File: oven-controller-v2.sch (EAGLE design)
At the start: 28 parts, among them Q1 IRFL310, Q2 IRFL310, U1 ARDUINO_SHIELDLONGPADS

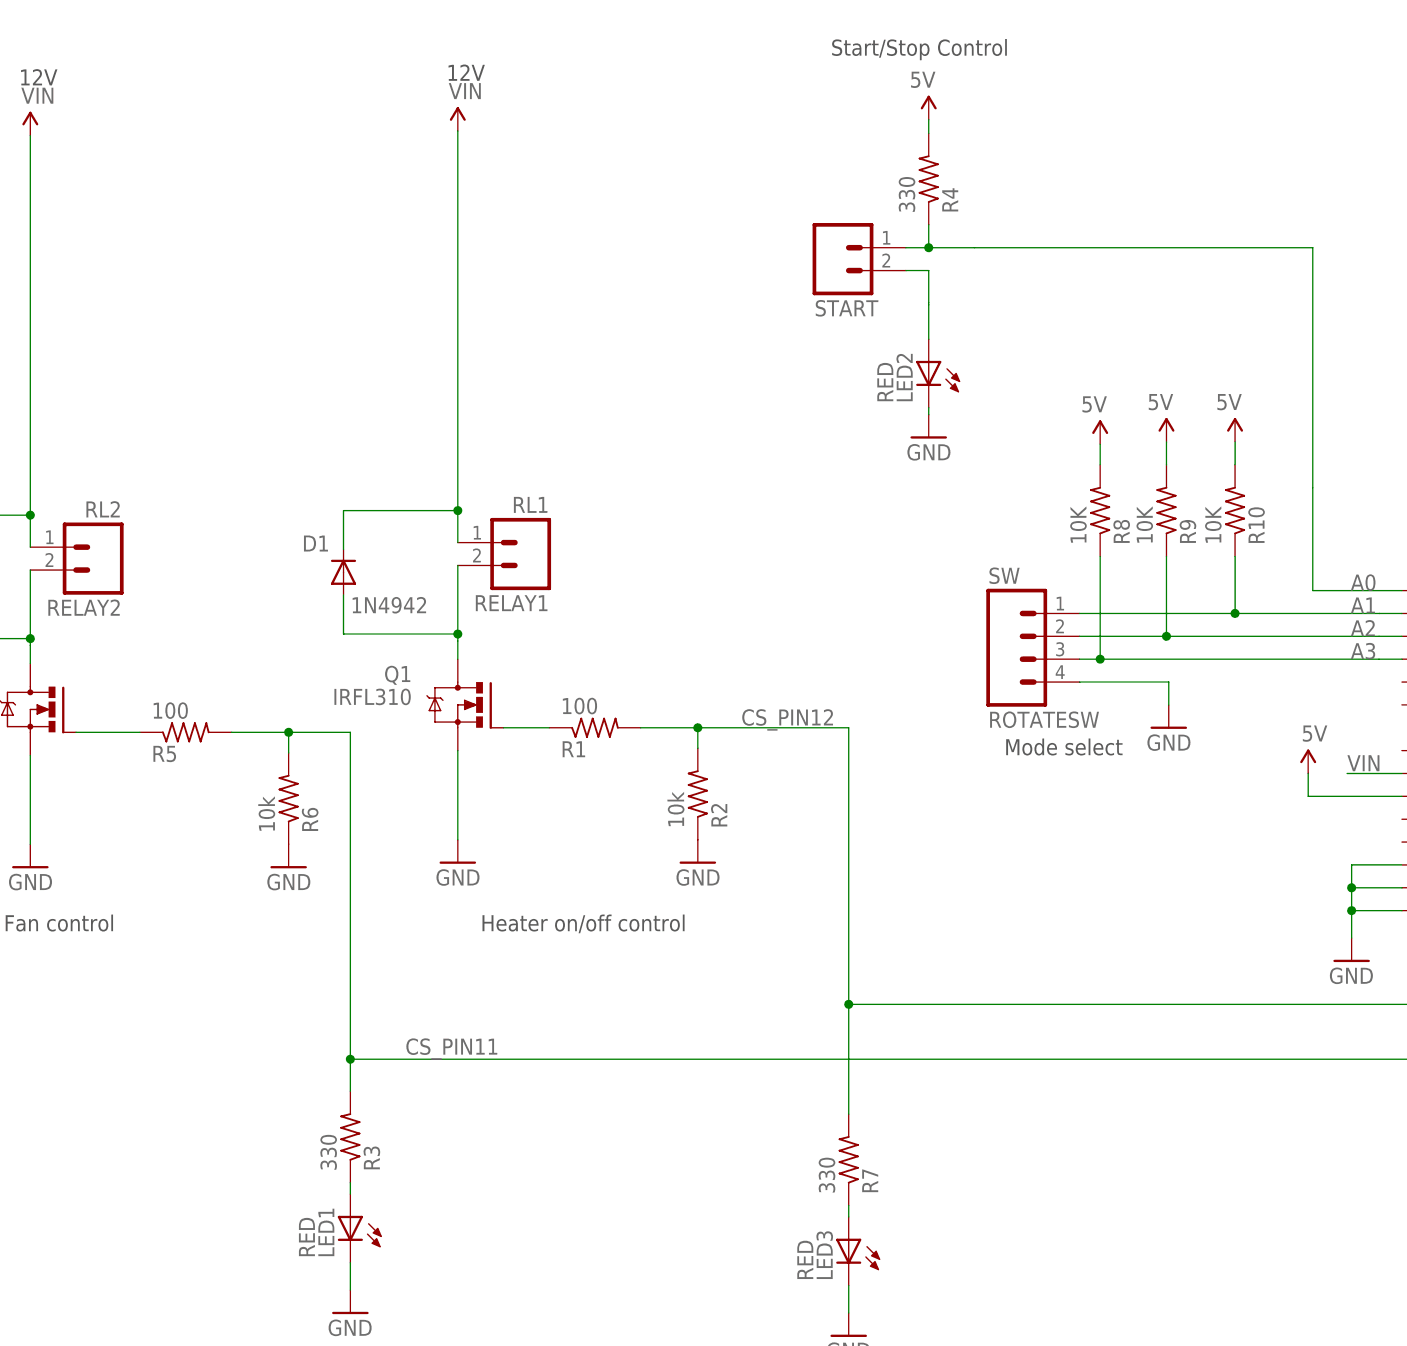
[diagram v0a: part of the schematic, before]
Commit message: Started board layout. Made resistors Sparkfun axial footprint.
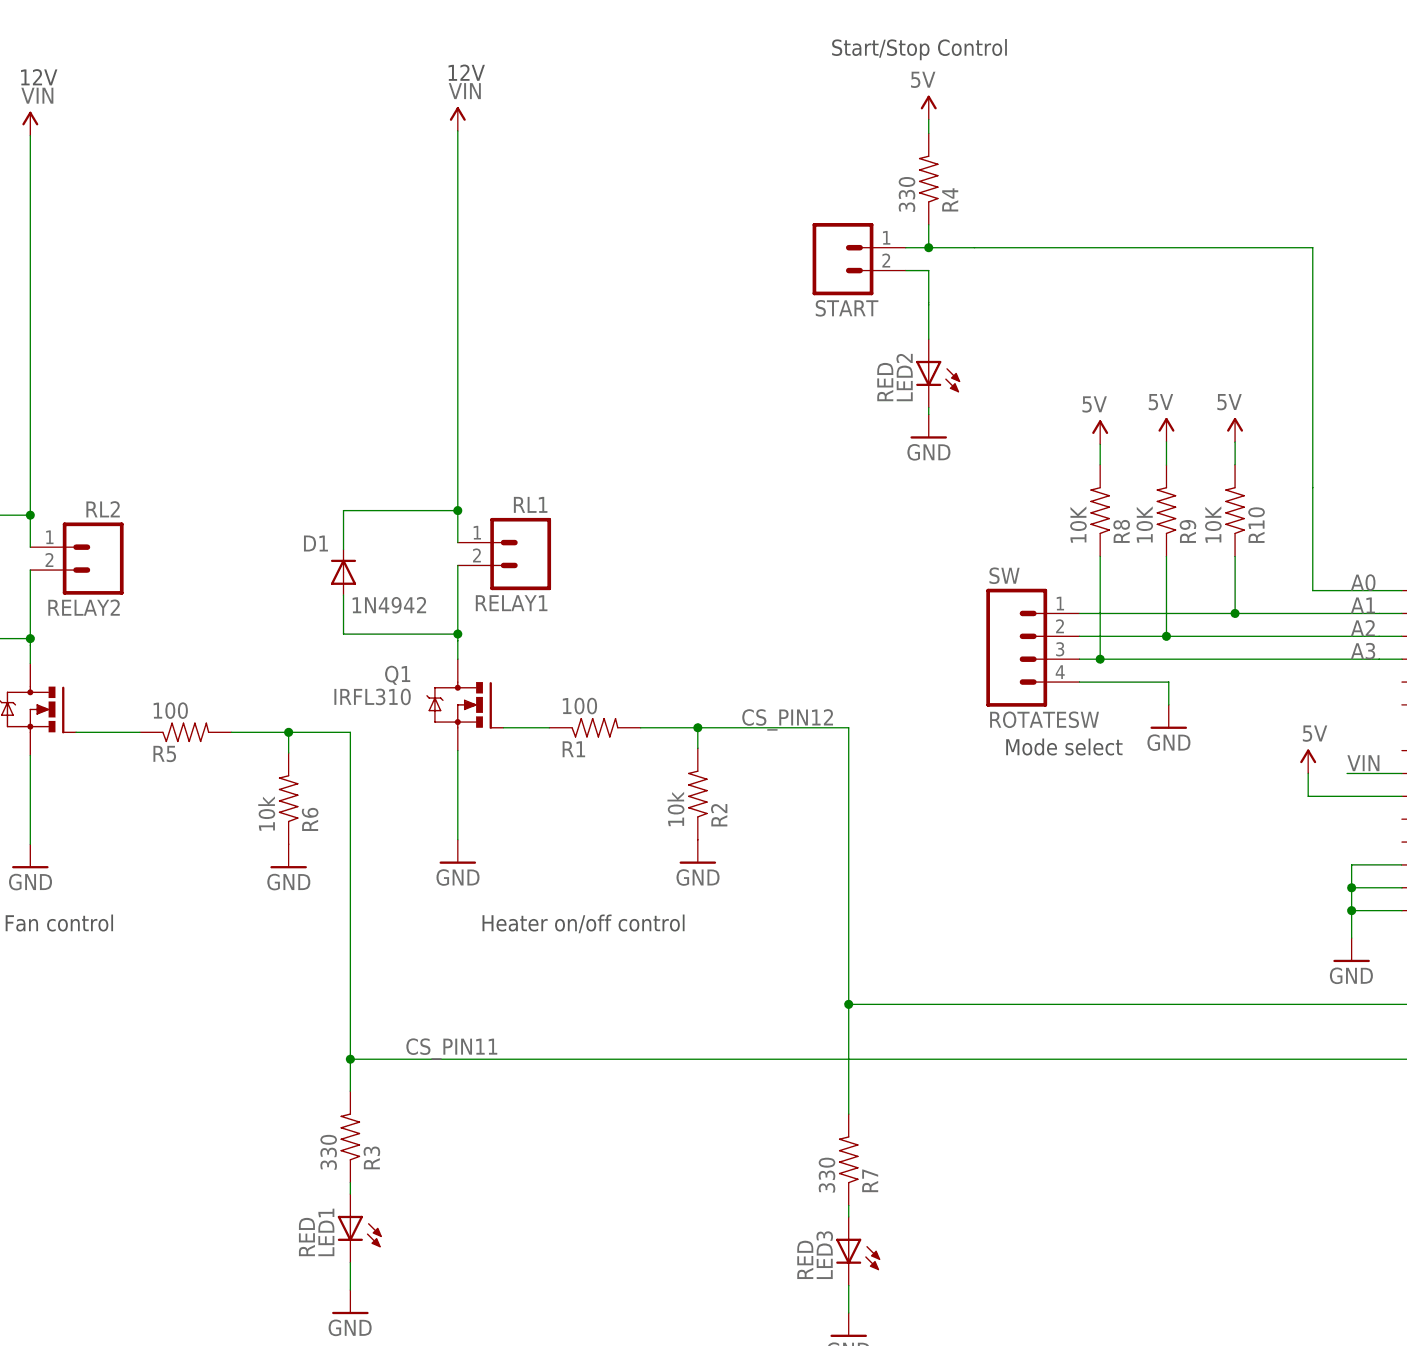
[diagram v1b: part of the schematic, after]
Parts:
- R1, R2, R5, R6: device resistor:R-US_V234/12 -> SparkFun-Passives:RESISTORAXIAL-0.3
- R10, R3, R4, R7, R8, R9: device resistor:R-US_0207/10 -> SparkFun-Passives:RESISTORAXIAL-0.3
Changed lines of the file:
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@@
 <setting verticaltext="up"/>
 </settings>
-<grid distance="0.1" unitdist="inch" unit="inch" style="lines" multiple="1" display="no" altdistance="0.01" altunitdist="inch" altunit="inch"/>
+<grid distance="0.01" unitdist="inch" unit="inch" style="dots" multiple="1" display="yes" altdistance="0.001" altunitdist="inch" altunit="inch"/>
 <layers>
 <layer number="1" name="Top" color="4" fill="11" visible="no" active="no"/>
@@
 <parts>
 <part name="Q1" library="transistor-power" deviceset="IRF520" device="" value="IRFL310"/>
-<part name="R1" library="resistor" deviceset="R-US_" device="V234/12" value="100"/>
-<part name="R2" library="resistor" deviceset="R-US_" device="V234/12" value="10k"/>
+<part name="R1" library="SparkFun-Passives" deviceset="RESISTOR" device="AXIAL-0.3" value="100"/>
+<part name="R2" library="SparkFun-Passives" deviceset="RESISTOR" device="AXIAL-0.3" value="10k"/>
 <part name="D1" library="diode" deviceset="1N4942" device=""/>
 <part name="GND1" library="supply1" deviceset="GND" device=""/>
@@
 <part name="GND7" library="supply1" deviceset="GND" device=""/>
 <part name="GND8" library="supply1" deviceset="GND" device=""/>
-<part name="R4" library="resistor" deviceset="R-US_" device="0207/10" value="330"/>
+<part name="R4" library="SparkFun-Passives" deviceset="RESISTOR" device="AXIAL-0.3" value="330"/>
 <part name="LED2" library="led" deviceset="LED" device="5MM" value="RED"/>
 <part name="GND10" library="supply1" deviceset="GND" device=""/>
@@
 <part name="ROTATESW" library="SparkFun-Connectors" deviceset="M04" device="LOCK_LONGPADS" value="SW"/>
 <part name="GND12" library="supply1" deviceset="GND" device=""/>
-<part name="R8" library="resistor" deviceset="R-US_" device="0207/10" value="10K"/>
-<part name="R9" library="resistor" deviceset="R-US_" device="0207/10" value="10K"/>
-<part name="R10" library="resistor" deviceset="R-US_" device="0207/10" value="10K"/>
+<part name="R8" library="SparkFun-Passives" deviceset="RESISTOR" device="AXIAL-0.3" value="10K"/>
+<part name="R9" library="SparkFun-Passives" deviceset="RESISTOR" device="AXIAL-0.3" value="10K"/>
+<part name="R10" library="SparkFun-Passives" deviceset="RESISTOR" device="AXIAL-0.3" value="10K"/>
 <part name="U$8" library="SparkFun-Aesthetics" deviceset="5V" device=""/>
 <part name="U$9" library="SparkFun-Aesthetics" deviceset="5V" device=""/>
@@
 <part name="RELAY2" library="SparkFun-Connectors" deviceset="M02" device="3.5MM_LOCK" value="RL2"/>
 <part name="U$14" library="SparkFun-Aesthetics" deviceset="VIN" device=""/>
-<part name="R5" library="resistor" deviceset="R-US_" device="V234/12" value="100"/>
-<part name="R6" library="resistor" deviceset="R-US_" device="V234/12" value="10k"/>
+<part name="R5" library="SparkFun-Passives" deviceset="RESISTOR" device="AXIAL-0.3" value="100"/>
+<part name="R6" library="SparkFun-Passives" deviceset="RESISTOR" device="AXIAL-0.3" value="10k"/>
 <part name="GND16" library="supply1" deviceset="GND" device=""/>
 <part name="LED1" library="led" deviceset="LED" device="5MM" value="RED"/>
-<part name="R3" library="resistor" deviceset="R-US_" device="0207/10" value="330"/>
+<part name="R3" library="SparkFun-Passives" deviceset="RESISTOR" device="AXIAL-0.3" value="330"/>
 <part name="GND9" library="supply1" deviceset="GND" device=""/>
 <part name="LED3" library="led" deviceset="LED" device="5MM" value="RED"/>
-<part name="R7" library="resistor" deviceset="R-US_" device="0207/10" value="330"/>
+<part name="R7" library="SparkFun-Passives" deviceset="RESISTOR" device="AXIAL-0.3" value="330"/>
 <part name="GND15" library="supply1" deviceset="GND" device=""/>
 </parts>

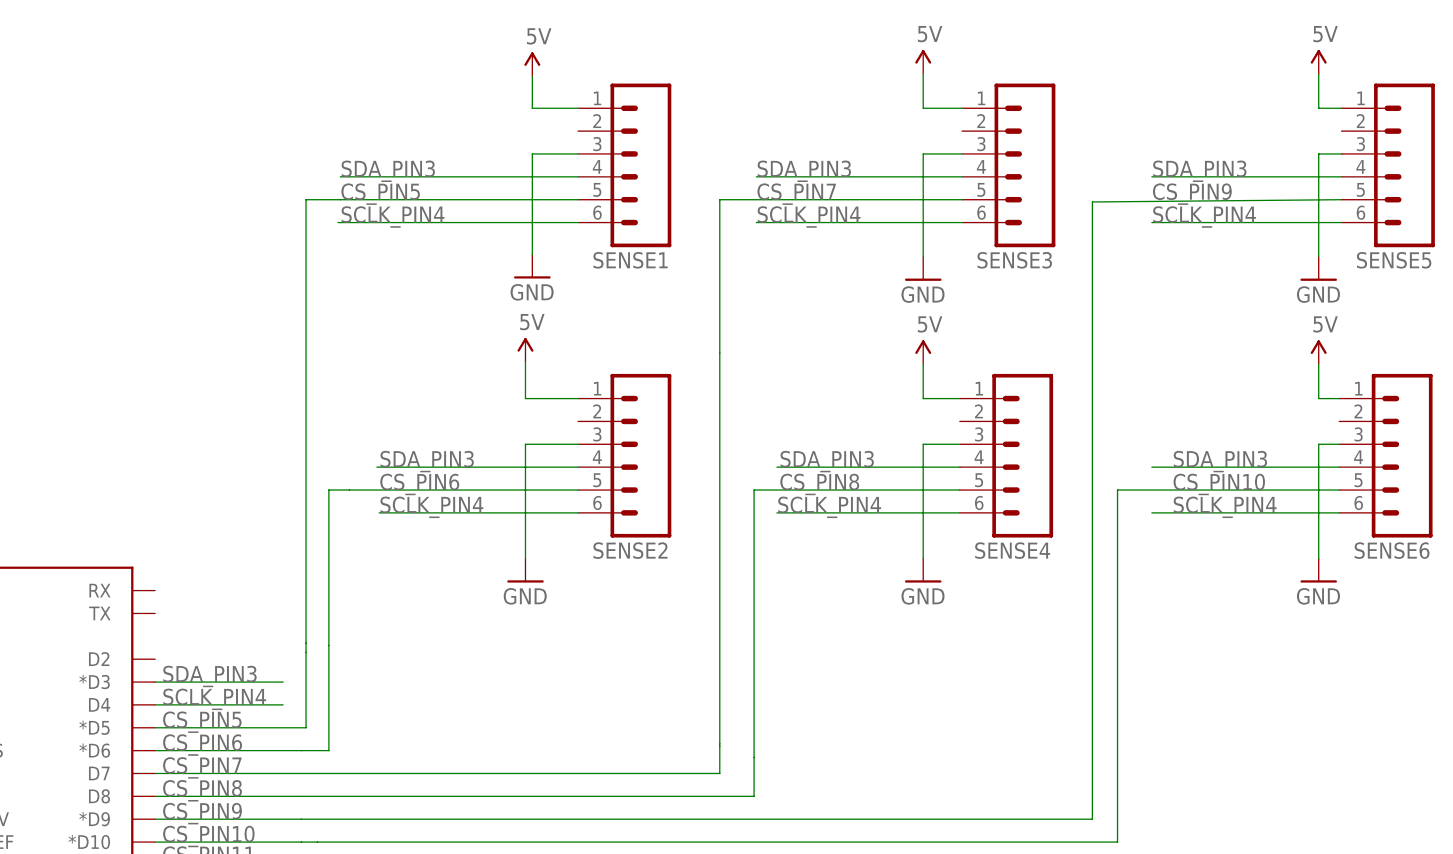
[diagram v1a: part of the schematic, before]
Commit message: Laid out board for v2. ERC and DRC good. Generated Gerbers.
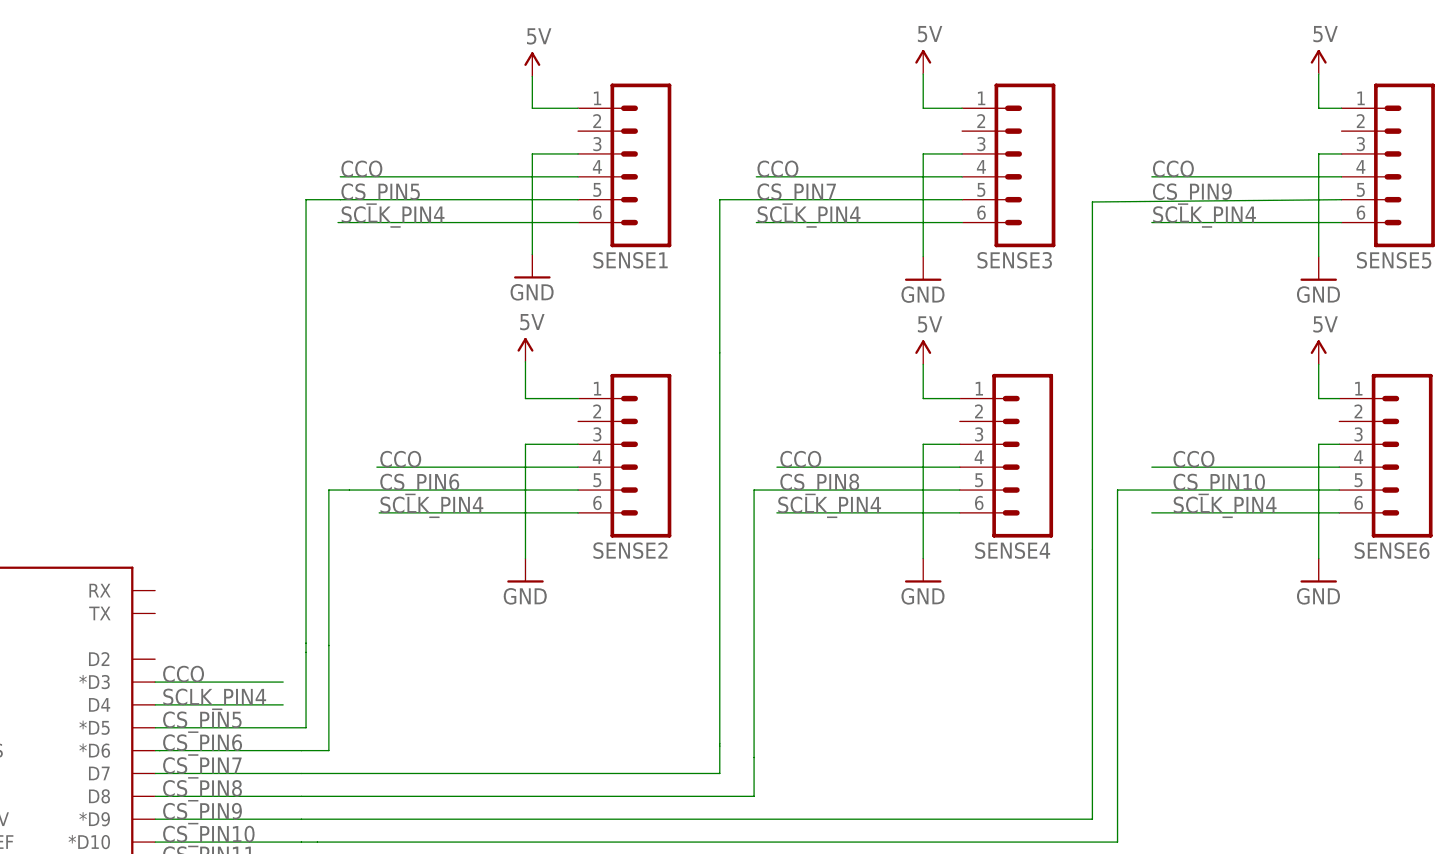
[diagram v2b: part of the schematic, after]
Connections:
- net SDA_PIN3 renamed CCO
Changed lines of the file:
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@@
 </segment>
 </net>
-<net name="SDA_PIN3" class="0">
+<net name="CCO" class="0">
 <segment>
 <wire x1="78.232" y1="45.974" x2="51.816" y2="45.974" width="0.1524" layer="91"/>
